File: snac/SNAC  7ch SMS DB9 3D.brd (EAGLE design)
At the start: 59.3 x 47.5 mm, 43 parts, among them IC1 4030D, K2 692112030100, Q1 BSS138, Q2 BSS138, Q3 BSS138, Q4 BSS138, Q5 BSS138, Q6 BSS138, Q7 BSS138, Q8 BSS138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

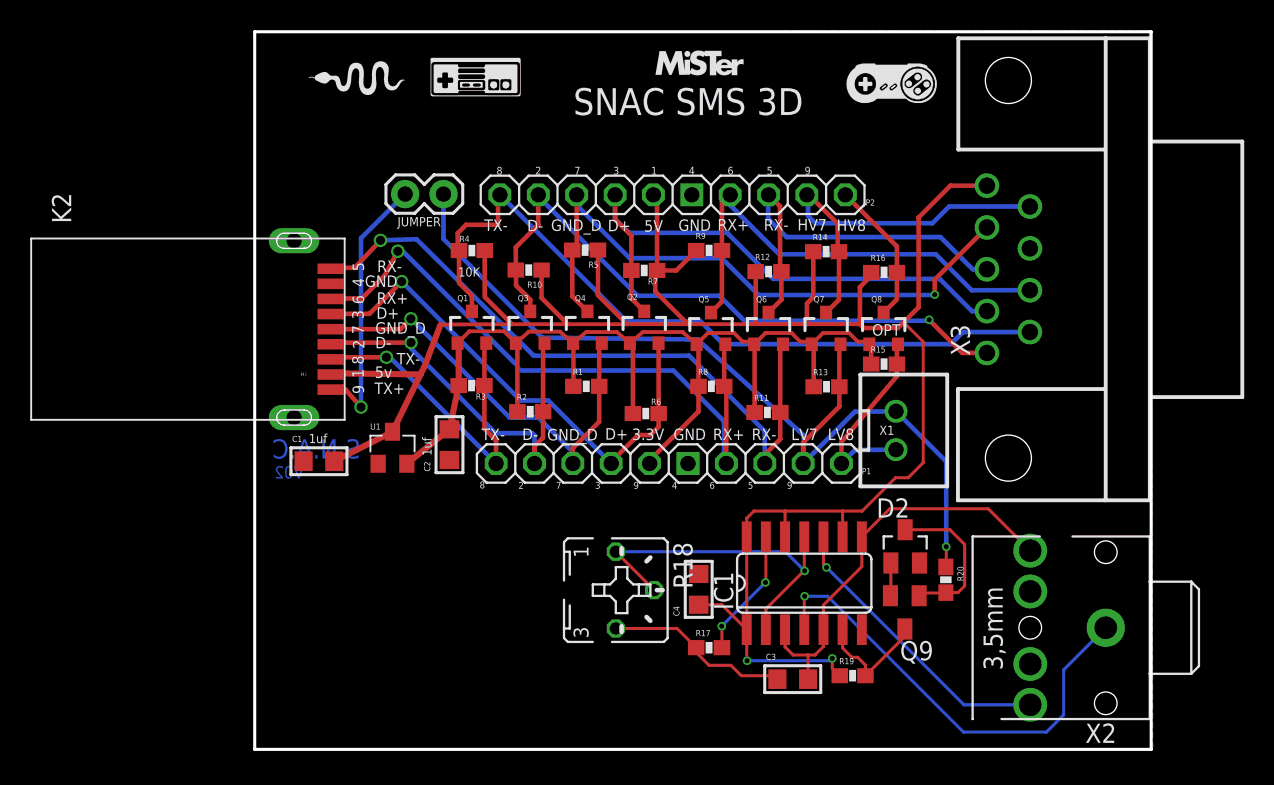
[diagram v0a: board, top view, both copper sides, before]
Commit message: Added combined voltage translation + SNES joyport
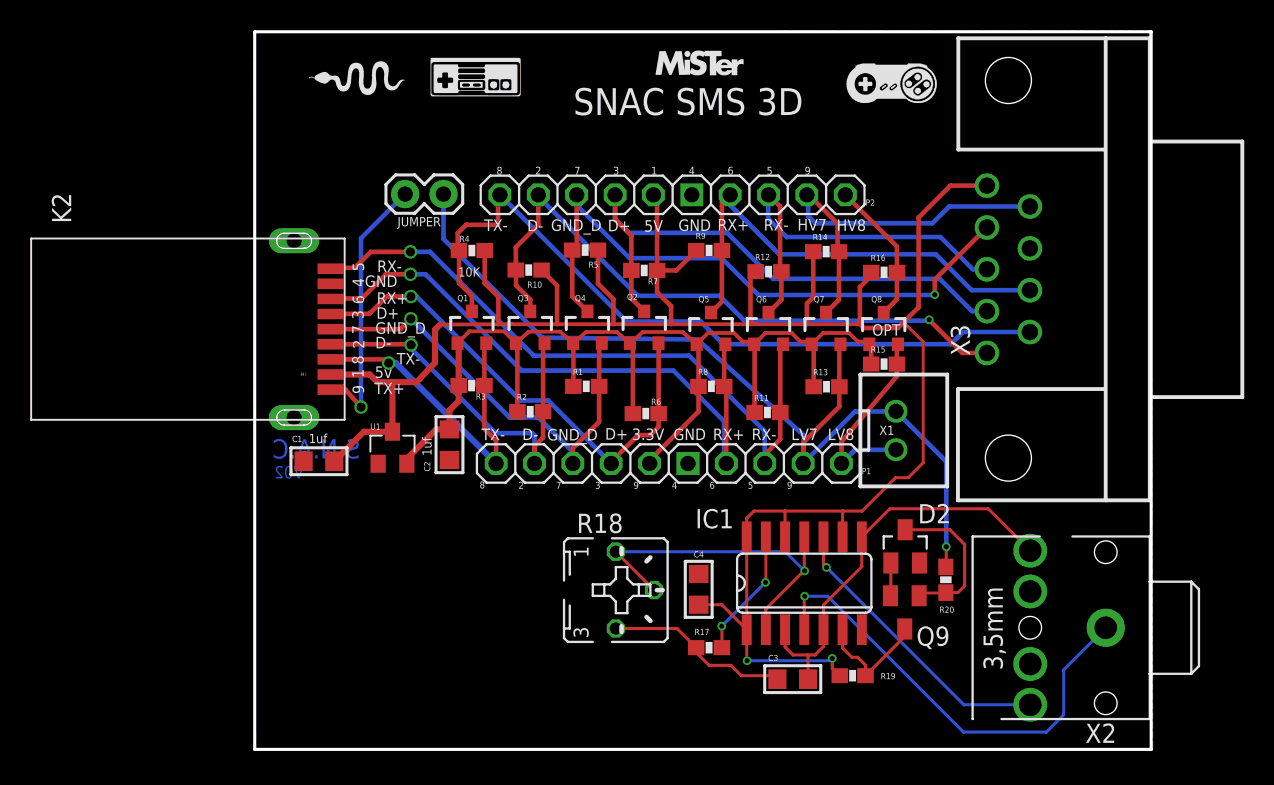
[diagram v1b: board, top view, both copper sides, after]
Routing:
- net LV5: track 43.4 -> 41.6 mm
- net HV: track 149.2 -> 148.2 mm
- net LV4: track 34.3 -> 33.4 mm
- net LV6: track 45.3 -> 44.7 mm
- net LV: track 71.9 -> 72.4 mm

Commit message: changed from LV7 to LV5 pin, for the 3D Glasses boards
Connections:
- net LV5: now also R20.1
- net LV7: no longer R20.1
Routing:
- net LV5: track 41.6 -> 59.6 mm, vias 1 -> 2
- net LV7: track 62.0 -> 50.3 mm, vias 1 -> 0
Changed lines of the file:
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@@
 <wire x1="5.08" y1="12.7" x2="5.08" y2="12.668" width="0.1778" layer="1"/>
 <via x="10.3378" y="14.3002" extent="1-16" drill="0.6"/>
-<wire x1="31.0896" y1="4.572" x2="31.0896" y2="1.9304" width="0.3048" layer="16"/>
-<wire x1="31.0896" y1="1.9304" x2="31.242" y2="1.778" width="0.1778" layer="16"/>
-<wire x1="27.7368" y1="7.9248" x2="17.7038" y2="7.9248" width="0.3048" layer="16"/>
-<wire x1="27.7368" y1="7.9248" x2="31.0896" y2="4.572" width="0.3048" layer="16"/>
+<wire x1="17.7038" y1="7.9248" x2="27.7368" y2="7.9248" width="0.3048" layer="16"/>
 <wire x1="31.176" y1="9.668" x2="31.1014" y2="9.5934" width="0.1778" layer="1"/>
 <wire x1="31.1014" y1="9.5934" x2="31.1014" y2="6.8834" width="0.3048" layer="1"/>
@@
 <wire x1="7.112" y1="12.7" x2="8.7122" y2="14.3002" width="0.3048" layer="1"/>
 <wire x1="8.7122" y1="14.3002" x2="10.3378" y2="14.3002" width="0.3048" layer="1"/>
+<contactref element="R20" pad="1"/>
+<wire x1="31.242" y1="4.4196" x2="31.242" y2="1.778" width="0.3048" layer="16"/>
+<wire x1="27.7368" y1="7.9248" x2="31.242" y2="4.4196" width="0.3048" layer="16"/>
+<wire x1="31.242" y1="1.778" x2="34.7726" y2="-1.7526" width="0.3048" layer="16"/>
+<wire x1="43.6626" y1="-1.7526" x2="45.72" y2="-3.81" width="0.3048" layer="16"/>
+<via x="45.72" y="-3.81" extent="1-16" drill="0.3302"/>
+<wire x1="34.7726" y1="-1.7526" x2="43.6626" y2="-1.7526" width="0.3048" layer="16"/>
+<wire x1="45.72" y1="-3.81" x2="45.7708" y2="-3.8608" width="0.3048" layer="1"/>
+<wire x1="45.7708" y1="-3.8608" x2="45.7708" y2="-5.0682" width="0.3048" layer="1"/>
 </signal>
 <signal name="HV5">
@@
 <wire x1="12.5222" y1="16.637" x2="12.5222" y2="19.6088" width="0.3048" layer="16"/>
 <wire x1="42.4688" y1="5.2324" x2="39.751" y2="5.207" width="0.3048" layer="16"/>
-<contactref element="R20" pad="1"/>
-<via x="45.7962" y="-3.7338" extent="1-16" drill="0.3302"/>
-<wire x1="45.7708" y1="-5.0682" x2="45.7962" y2="-5.0428" width="0.2032" layer="1"/>
-<wire x1="45.7962" y1="-5.0428" x2="45.7962" y2="-3.7338" width="0.2032" layer="1"/>
-<wire x1="42.4688" y1="5.2324" x2="45.7962" y2="1.905" width="0.3048" layer="16"/>
-<wire x1="45.7962" y1="1.905" x2="45.7962" y2="-3.7338" width="0.3048" layer="16"/>
 </signal>
 <signal name="HV7">
